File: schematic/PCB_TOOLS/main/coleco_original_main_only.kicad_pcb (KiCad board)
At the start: 2 copper layers, 168.4 x 213.9 mm, 196 parts, among them J0 Conn_01x04, J1 Cartridge Port, J2 Expansion Port, J4A1 Conn_01x08, J5 Player 1, J6 Player 2, Q2 2N3906, Q3 2N3906, Q4 2N3904, Q5 2N3904, Q6 2N3906, U1 Z80CPU, U10 MK4116P, U11 MK4116P, U12 MK4116P, U13 MK4116P, U14 MK4116P, U15 MK4116P, U16 MK4116P, U17 MK4116P, U18 74LS541, U19 74LS541, U2 27C256, U20 SN76489AN, U22 74LS04, U23 4066, U24 74LS00, U3 SCM2114AL, U4 SCM2114AL, U5 74LS138, U6 74LS138, U7 74LS05, U8 74LS74, U9 TMS9928A, Y1 7.159090Mhz

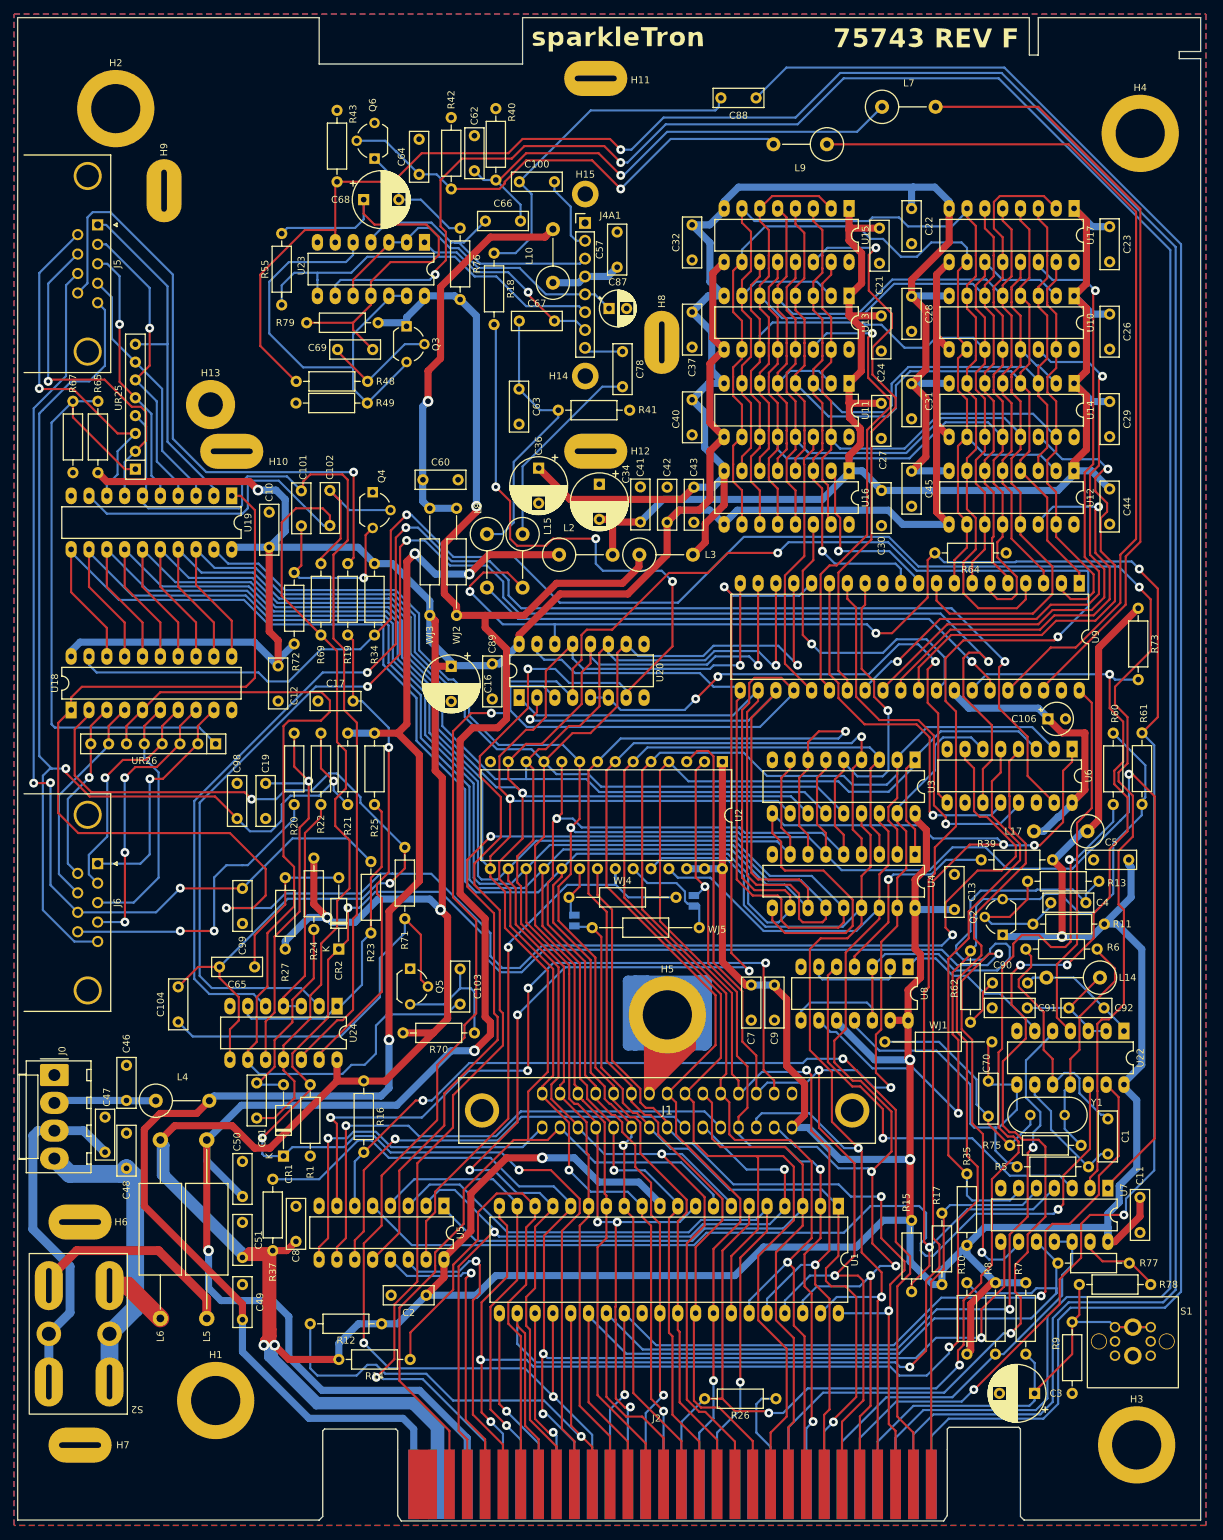
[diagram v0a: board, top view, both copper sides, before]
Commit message: remove solder mask from edge connector (thanks to Tekman@AtariAge for pointing this out), update gerbers and version
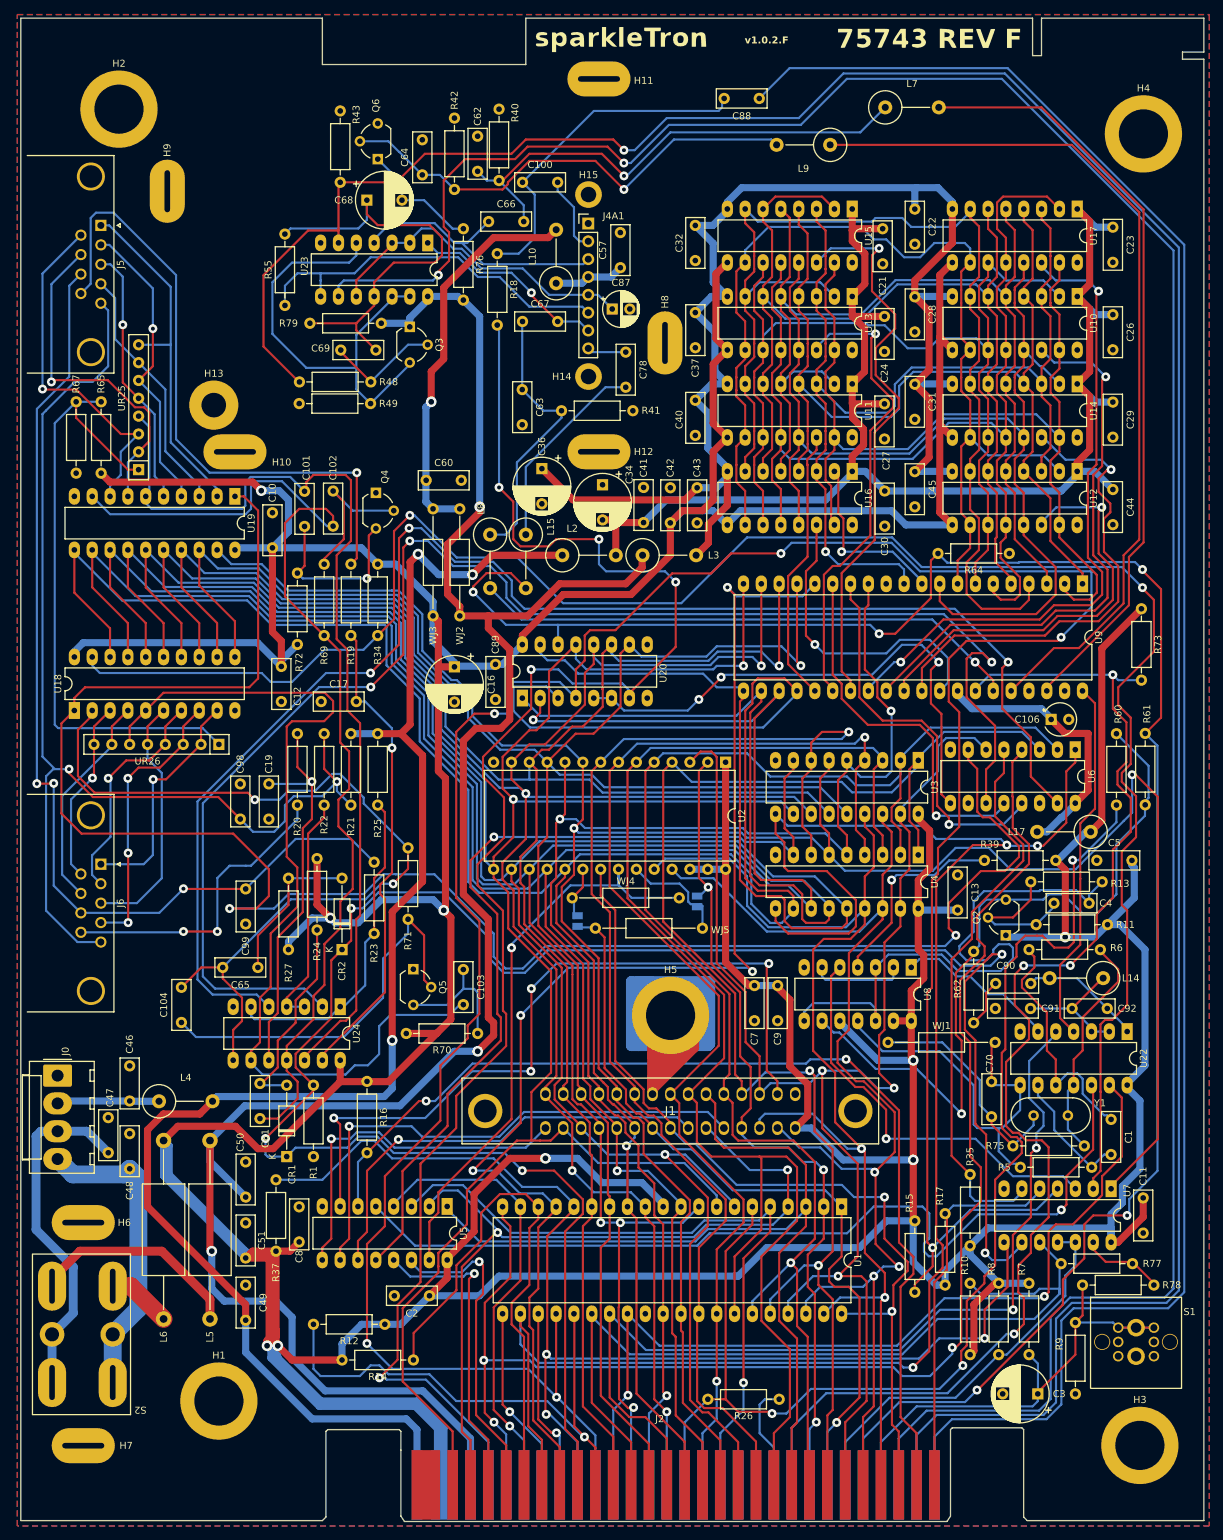
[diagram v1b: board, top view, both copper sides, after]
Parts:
- moved C101 0.46 mm to (64.2, 89.1)
- moved C1 0.46 mm to (179.0, 173.5)
- moved C10 0.46 mm to (59.6, 92.1)
- moved C100 0.46 mm to (95.2, 40.1)
- moved C102 0.46 mm to (68.3, 84.0)
- moved C103 0.46 mm to (86.8, 152.1)
- moved C104 0.46 mm to (46.7, 159.7)
- moved C106 0.46 mm to (170.5, 116.5)
- moved C11 0.46 mm to (183.6, 189.7)
- moved C12 0.46 mm to (60.9, 109.0)
- moved C13 0.46 mm to (157.2, 138.7)
- moved C16 0.46 mm to (85.5, 109.1)
- moved C17 0.46 mm to (66.6, 114.0)
- moved C19 0.46 mm to (59.1, 130.7)
- moved C2 0.46 mm to (82.0, 198.6)
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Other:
- board text added: "v1.0.2.F"
